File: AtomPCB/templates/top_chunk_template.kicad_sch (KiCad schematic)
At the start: 8 parts, among them J2 DF40C-40DP-0.4V_51_, U1 ATtiny416-M, U6 MPM3610AGQV-P

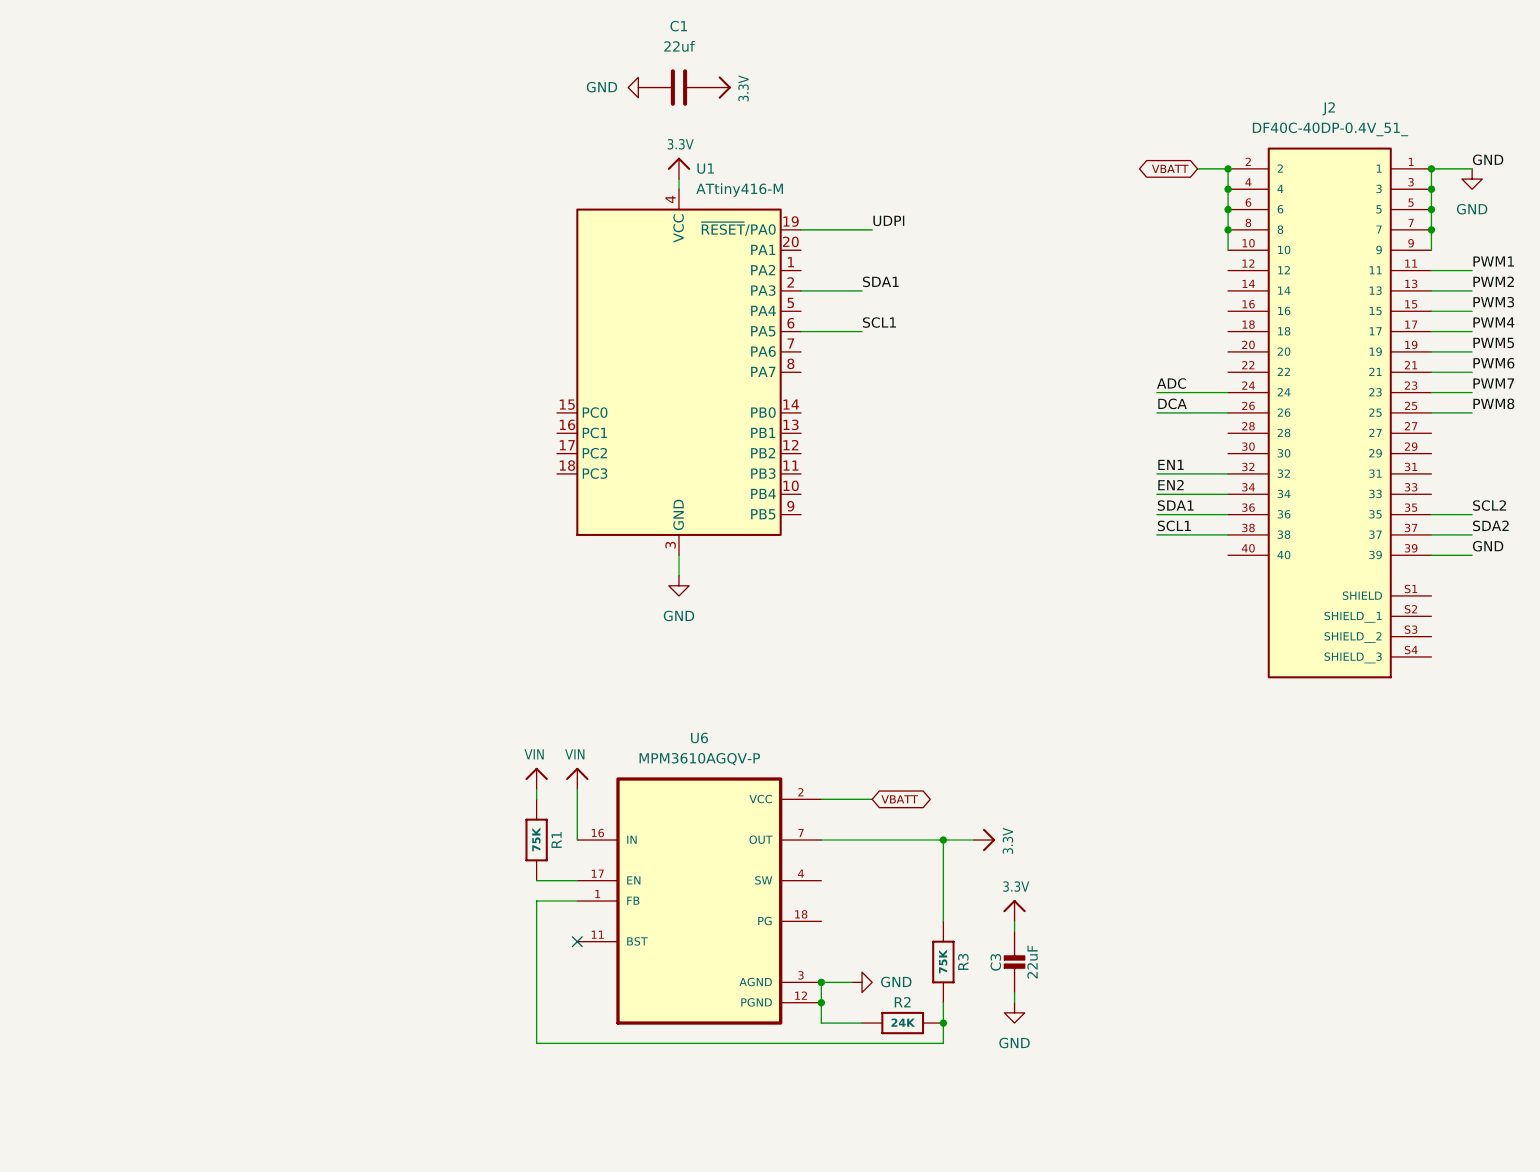
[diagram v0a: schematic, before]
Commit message: first pcb panel order placed!
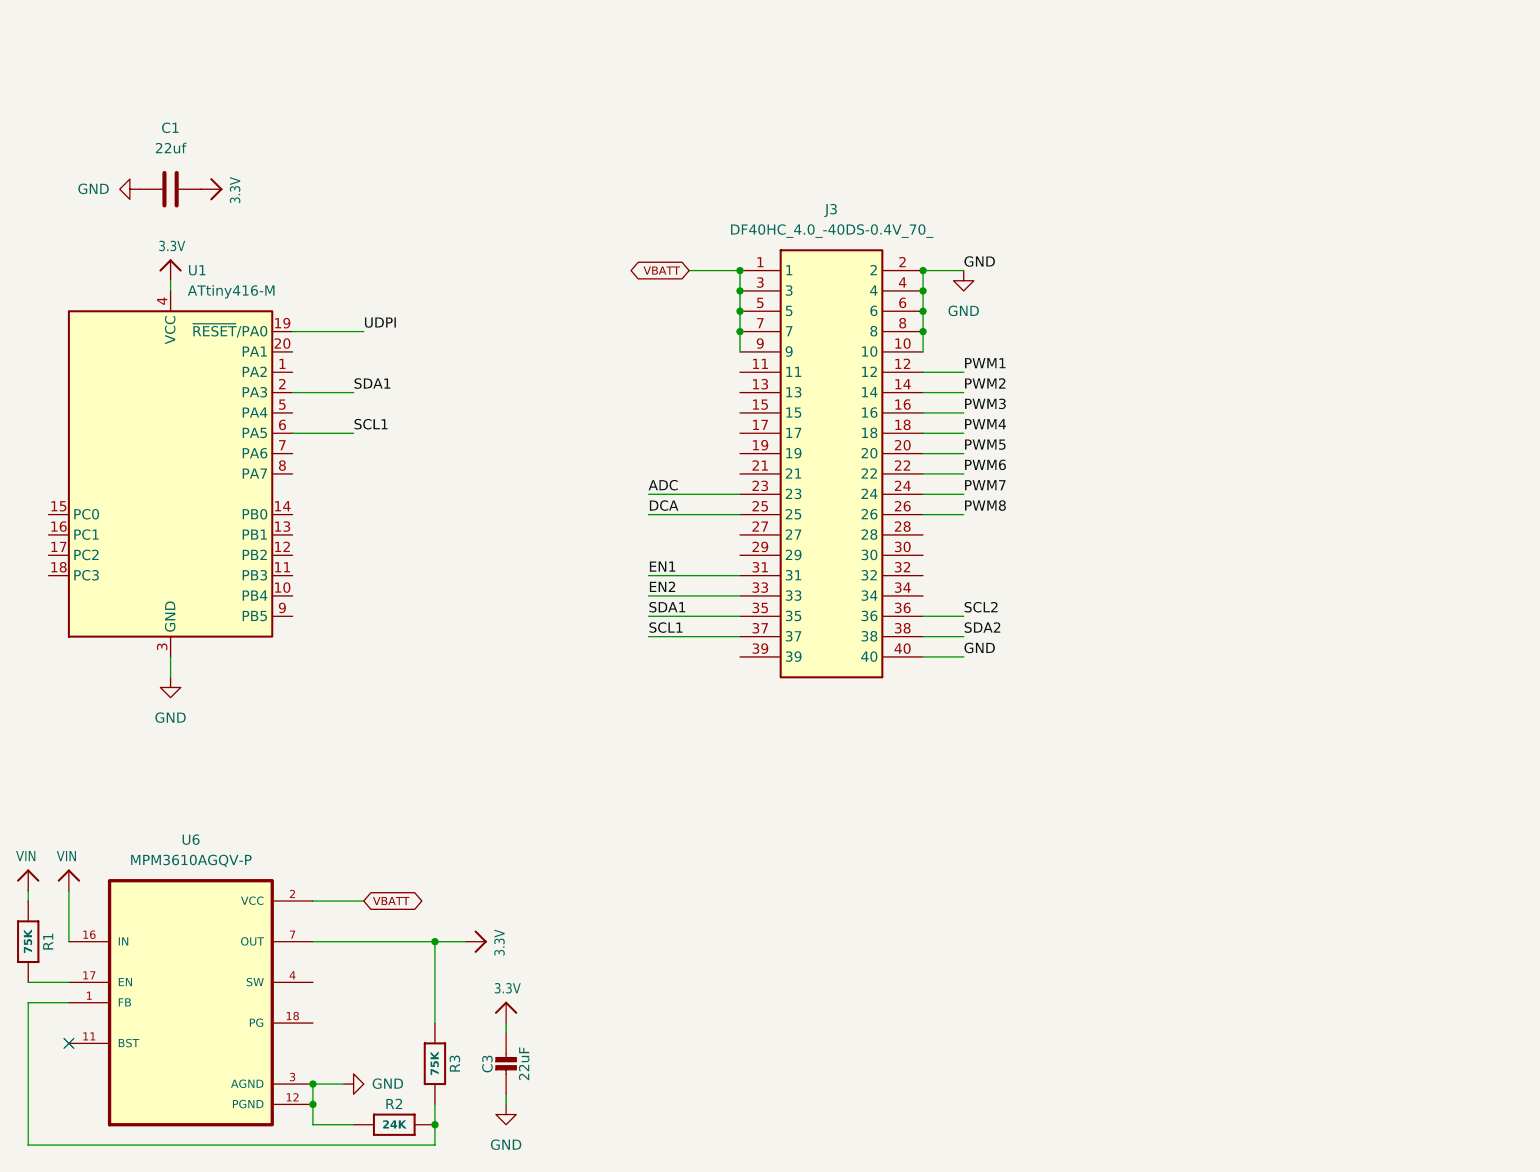
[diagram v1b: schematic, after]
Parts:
- removed J2: DF40C-40DP-0.4V_51_, DF40C-40DP-0.4V_51_:HRS_DF40C-40DP-0.4V_51_, symbol DF40C40DP_0_4V_51:DF40C-40DP-0.4V_51_
- added J3: DF40HC_4.0_-40DS-0.4V_70_, HIROSE_DF40HC_40_connector:DF40HC4040DS04V70, symbol HIROSE_DF40HC_40_connector:DF40HC_4.0_-40DS-0.4V_70_
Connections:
- net ADC: now also J3.23
- net DCA: now also J3.25
- net EN1: now also J3.31
- net EN2: now also J3.33
- net GND: now also J3.10, J3.2, J3.4, J3.40, J3.6, J3.8
- net PWM1: now also J3.12
- net PWM2: now also J3.14
- net PWM3: now also J3.16
- net PWM4: now also J3.18
- net PWM5: now also J3.20
- net PWM6: now also J3.22
- net PWM7: now also J3.24
- net PWM8: now also J3.26
- net SCL1: now also J3.37
- net SCL2: now also J3.36
- net SDA1: now also J3.35
- net SDA2: now also J3.38
- net VBATT: now also J3.1, J3.3, J3.5, J3.7, J3.9
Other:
- moved on the sheet: C1, C3, R1, R2, R3, U1, U6
